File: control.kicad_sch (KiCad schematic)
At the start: 25 parts, among them U1 MX6UL-VM, Y1 24Mhz, Y2 32.768kHz

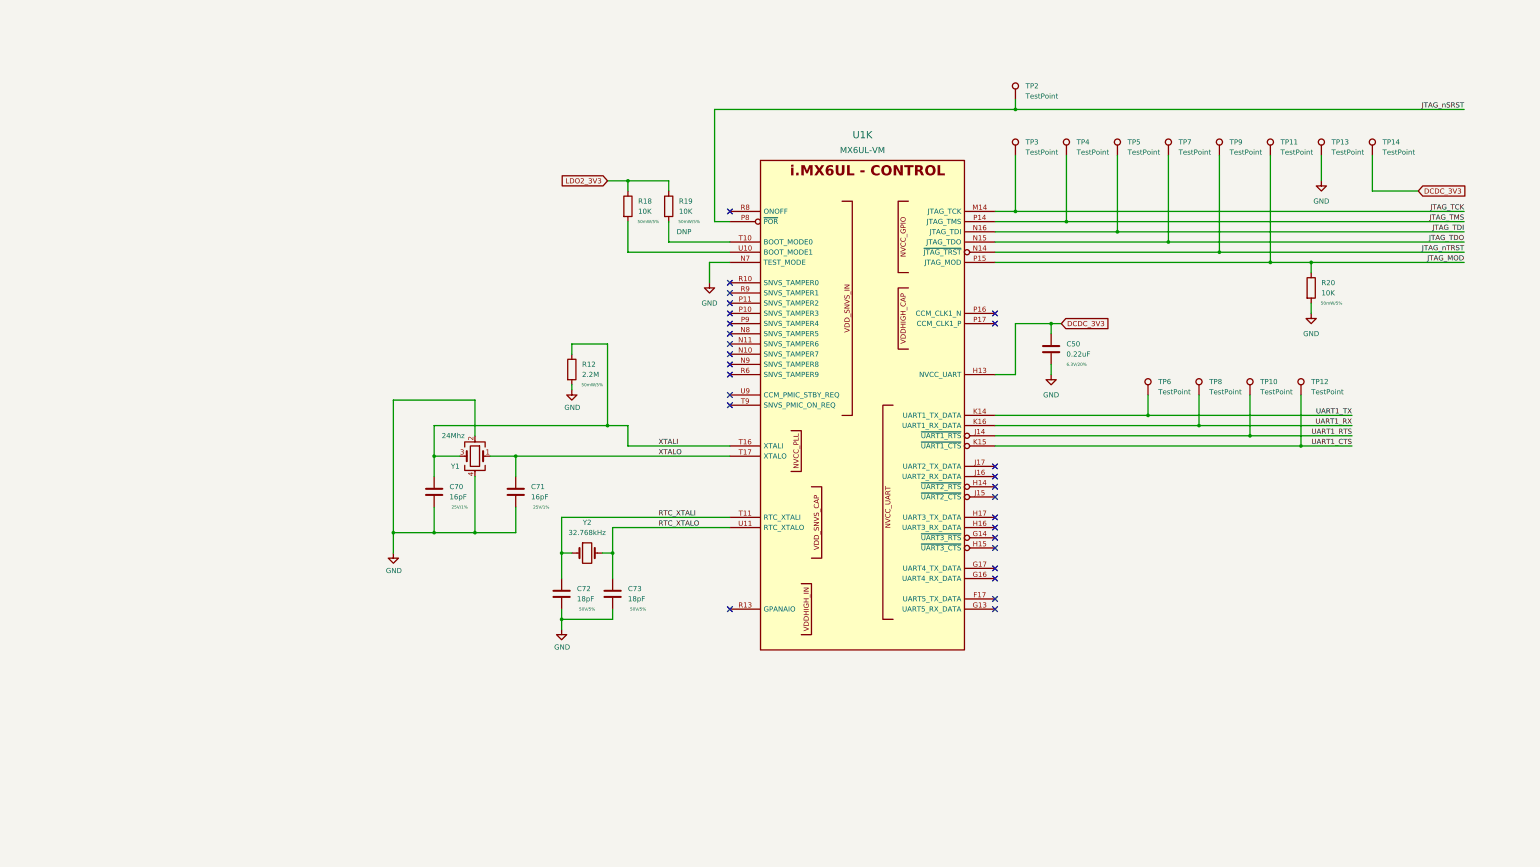
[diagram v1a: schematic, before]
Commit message: start moving to hierarchal labels, add emmc
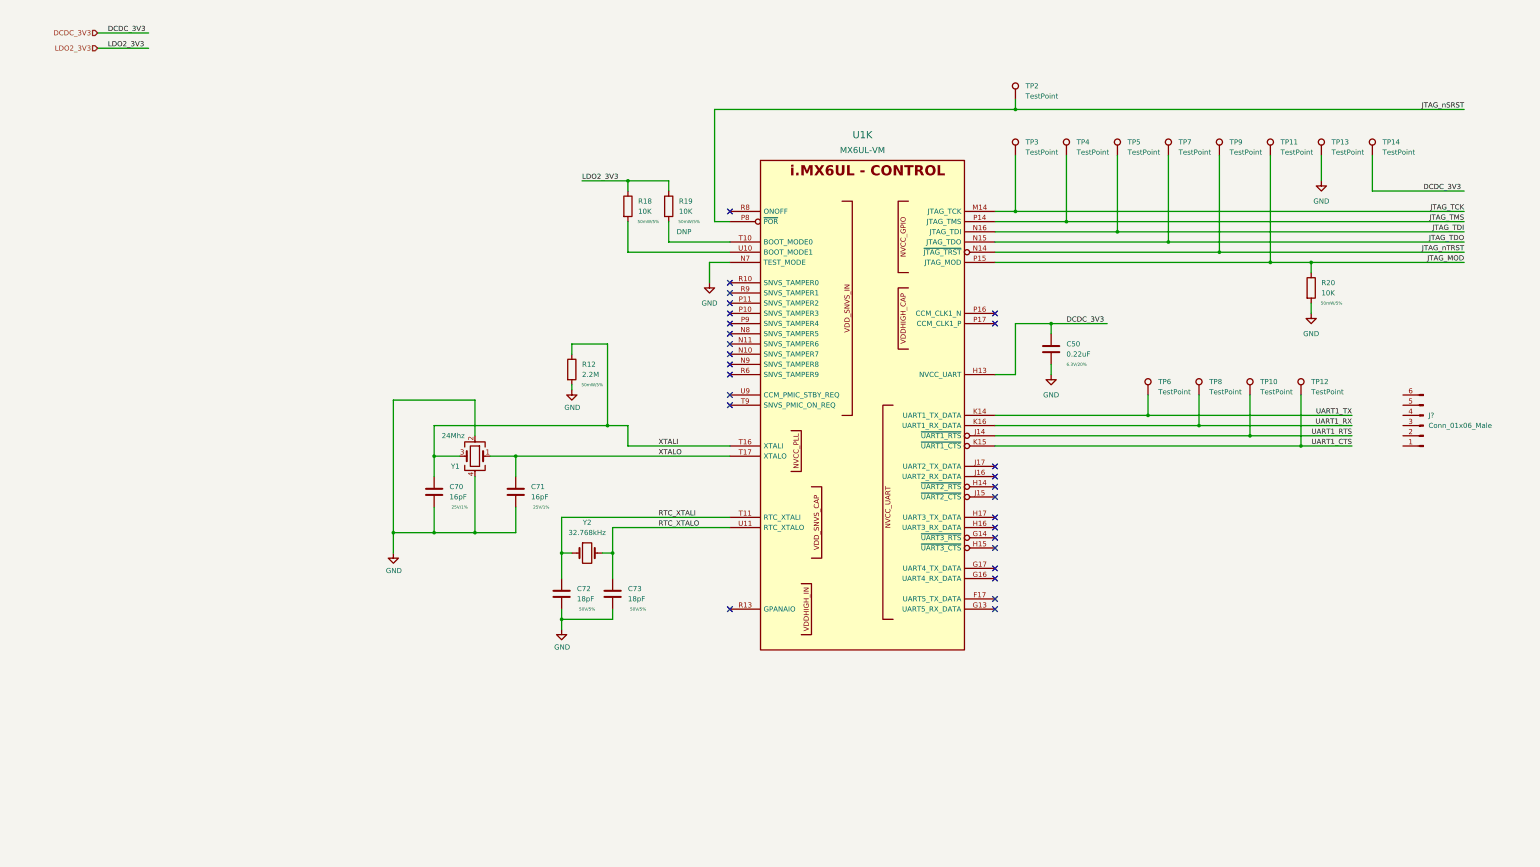
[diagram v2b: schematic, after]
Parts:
- added J?: Conn_01x06_Male, symbol Connector:Conn_01x06_Male
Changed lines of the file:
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@@
     (stroke (width 0) (type default) (color 0 0 0 0))
   )
-  (wire (pts (xy 361.95 60.96) (xy 350.52 60.96))
+  (wire (pts (xy 350.52 60.96) (xy 373.38 60.96))
     (stroke (width 0) (type default) (color 0 0 0 0))
   )
@@
     (stroke (width 0) (type default) (color 0 0 0 0))
   )
+  (wire (pts (xy 33.02 21.59) (xy 45.72 21.59))
+    (stroke (width 0) (type default) (color 0 0 0 0))
+  )
   (wire (pts (xy 294.64 111.76) (xy 294.64 116.84))
     (stroke (width 0) (type default) (color 0 0 0 0))
@@
     (stroke (width 0) (type default) (color 0 0 0 0))
   )
-  (wire (pts (xy 160.02 58.42) (xy 165.1 58.42))
+  (wire (pts (xy 153.67 58.42) (xy 165.1 58.42))
     (stroke (width 0) (type default) (color 0 0 0 0))
   )
@@
     (stroke (width 0) (type default) (color 0 0 0 0))
   )
-  (wire (pts (xy 273.05 93.98) (xy 270.51 93.98))
+  (wire (pts (xy 270.51 93.98) (xy 284.48 93.98))
     (stroke (width 0) (type default) (color 0 0 0 0))
   )
@@
   )
   (wire (pts (xy 270.51 93.98) (xy 261.62 93.98))
+    (stroke (width 0) (type default) (color 0 0 0 0))
+  )
+  (wire (pts (xy 33.02 25.4) (xy 45.72 25.4))
     (stroke (width 0) (type default) (color 0 0 0 0))
   )
@@
     (effects (font (size 1.27 1.27)) (justify right bottom))
   )
+  (label "DCDC_3V3" (at 363.22 60.96 0)
+    (effects (font (size 1.27 1.27)) (justify left bottom))
+  )
   (label "UART1_TX" (at 345.44 116.84 180)
     (effects (font (size 1.27 1.27)) (justify right bottom))
@@
     (effects (font (size 1.27 1.27)) (justify left bottom))
   )
+  (label "LDO2_3V3" (at 153.67 58.42 0)
+    (effects (font (size 1.27 1.27)) (justify left bottom))
+  )
   (label "UART1_RX" (at 345.44 119.38 180)
     (effects (font (size 1.27 1.27)) (justify right bottom))
@@
   (label "UART1_CTS" (at 345.44 124.46 180)
     (effects (font (size 1.27 1.27)) (justify right bottom))
+  )
+  (label "DCDC_3V3" (at 274.32 93.98 0)
+    (effects (font (size 1.27 1.27)) (justify left bottom))
   )
   (label "RTC_XTALO" (at 172.72 144.78 0)
@@
     (effects (font (size 1.27 1.27)) (justify right bottom))
   )
-  (global_label "DCDC_3V3" (shape input) (at 273.05 93.98 0) (fields_autoplaced)
-    (effects (font (size 1.27 1.27)) (justify left))
-    (property "Intersheet References" "${INTERSHEET_REFS}" (id 0) (at 285.0183 93.9006 0)
-      (effects (font (size 1.27 1.27)) (justify left) hide)
-    )
-  )
-  (global_label "LDO2_3V3" (shape input) (at 160.02 58.42 180) (fields_autoplaced)
+  (label "DCDC_3V3" (at 35.56 21.59 0)
+    (effects (font (size 1.27 1.27)) (justify left bottom))
+  )
+  (label "LDO2_3V3" (at 35.56 25.4 0)
+    (effects (font (size 1.27 1.27)) (justify left bottom))
+  )
+  (hierarchical_label "LDO2_3V3" (shape input) (at 33.02 25.4 180)
     (effects (font (size 1.27 1.27)) (justify right))
-    (property "Intersheet References" "${INTERSHEET_REFS}" (id 0) (at 148.2936 58.3406 0)
-      (effects (font (size 1.27 1.27)) (justify right) hide)
-    )
-  )
-  (global_label "DCDC_3V3" (shape input) (at 361.95 60.96 0) (fields_autoplaced)
-    (effects (font (size 1.27 1.27)) (justify left))
-    (property "Intersheet References" "${INTERSHEET_REFS}" (id 0) (at 373.9183 60.8806 0)
-      (effects (font (size 1.27 1.27)) (justify left) hide)
-    )
+  )
+  (hierarchical_label "DCDC_3V3" (shape input) (at 33.02 21.59 180)
+    (effects (font (size 1.27 1.27)) (justify right))
   )
   (symbol (lib_id "Device:R") (at 151.13 105.41 0) (unit 1)
@@
     (pin "1")
   )
+  (symbol (lib_id "Connector:Conn_01x06_Male") (at 363.22 119.38 180) (unit 1)
+    (in_bom yes) (on_board yes) (fields_autoplaced)
+    (property "Reference" "J?" (id 0) (at 364.49 116.8399 0)
+      (effects (font (size 1.27 1.27)) (justify right))
+    )
+    (property "Value" "Conn_01x06_Male" (id 1) (at 364.49 119.3799 0)
+      (effects (font (size 1.27 1.27)) (justify right))
+    )
+    (property "Footprint" "" (id 2) (at 363.22 119.38 0)
+      (effects (font (size 1.27 1.27)) hide)
+    )
+    (property "Datasheet" "~" (id 3) (at 363.22 119.38 0)
+      (effects (font (size 1.27 1.27)) hide)
+    )
+    (pin "1")
+    (pin "2")
+    (pin "3")
+    (pin "4")
+    (pin "5")
+    (pin "6")
+  )
   (symbol (lib_id "Device:R") (at 165.1 64.77 0) (unit 1)

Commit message: move to hierarchal labels, work on power tree, add basic pcb layout
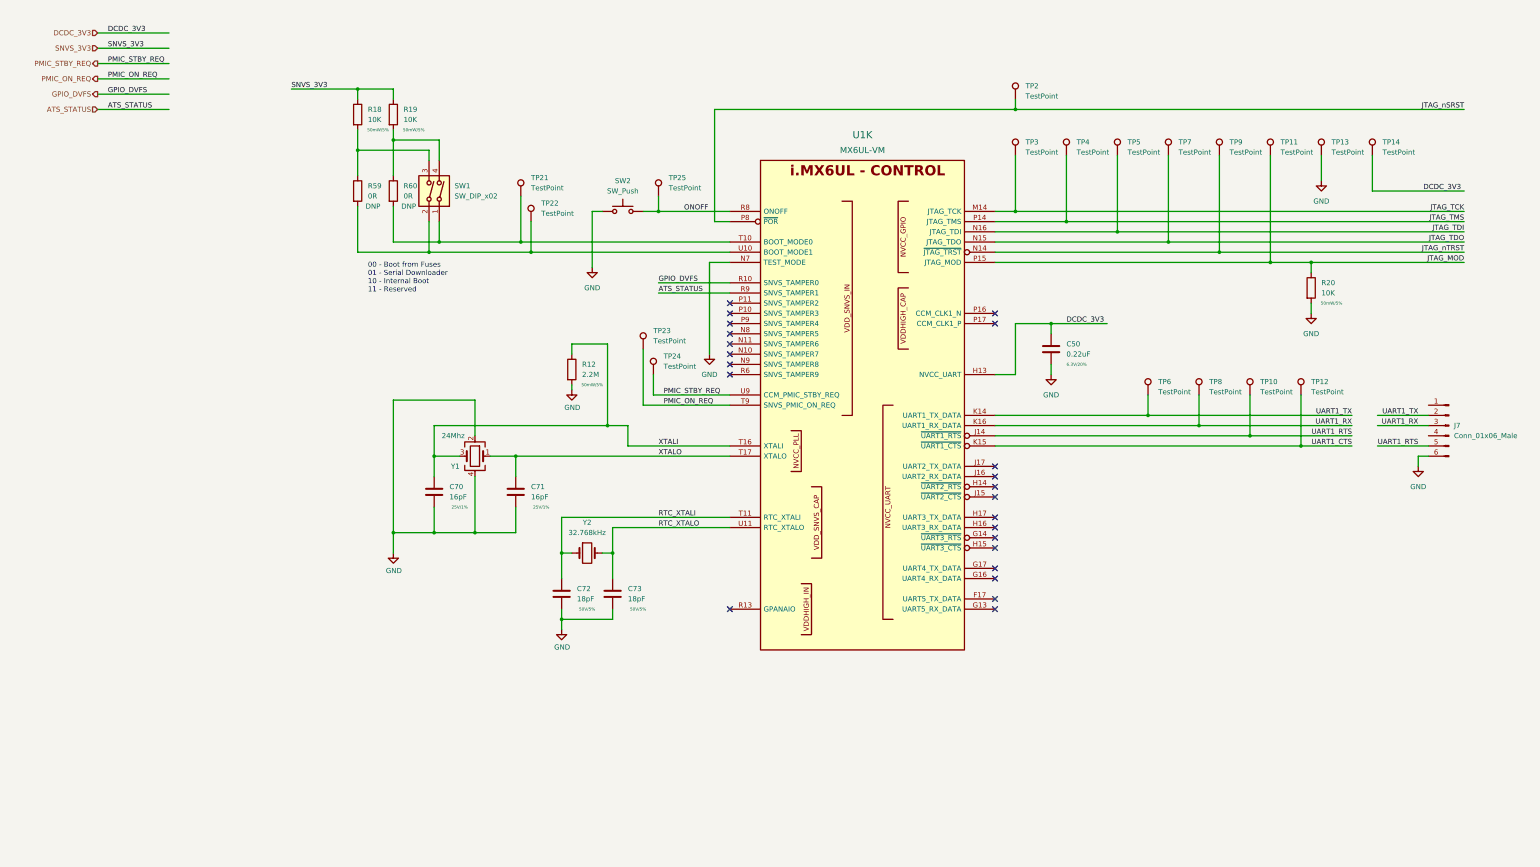
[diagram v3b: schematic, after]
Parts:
- added R59, R60: 0R, Resistor_SMD:R_0402_1005Metric, symbol Device:R
- added SW1: SW_DIP_x02, symbol Switch:SW_DIP_x02
- added SW2: SW_Push, symbol Switch:SW_Push
- added TP21, TP22, TP23, TP24, TP25: TestPoint, TestPoint:TestPoint_Pad_D1.0mm, symbol Connector:TestPoint
- C50: footprint Capacitor_SMD:C_0402_1005Metric -> Capacitor_SMD:C_0201_0603Metric
- J7: renamed from J?; footprint (none) -> Connector_PinHeader_2.54mm:PinHeader_1x06_P2.54mm_Vertical_SMD_Pin1Left
- R19: DNP DNP -> (none)
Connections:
- net GND: now also J7.6 (Pin_6), SW2.1
- net UART1_RTS: now also J7.5 (Pin_5)
- net UART1_RX: now also J7.3 (Pin_3)
- net UART1_TX: now also J7.2 (Pin_2)
- net at U1.T10 (BOOT_MODE0): now also R60.2, SW1.1, TP21.1; no longer R19.2
- net GPIO_DVFS: now reaches U1.R10 (SNVS_TAMPER0)
- net ONOFF: now reaches U1.R8 (ONOFF)
- net ONOFF: now also SW2.2, TP25.1
- net ATS_STATUS: now reaches U1.R9 (SNVS_TAMPER1)
- net PMIC_ON_REQ: now reaches U1.T9 (SNVS_PMIC_ON_REQ)
- net PMIC_ON_REQ: now also TP23.1
- net at U1.U10 (BOOT_MODE1): now also R59.2, SW1.2, TP22.1; no longer R18.2
- net PMIC_STBY_REQ: now reaches U1.U9 (CCM_PMIC_STBY_REQ)
- net PMIC_STBY_REQ: now also TP24.1
- net LDO2_3V3 renamed SNVS_3V3
- new net: R19.2, R60.1, SW1.4
- new net: R18.2, R59.1, SW1.3
- no-connect marks 28 -> 23
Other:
- note added: "00 - Boot from Fuses 01 - Serial Downloader 10 - Internal Boot 11 - Reserved"
- moved on the sheet: J7, R18, R19

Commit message: most of sch done, inital component pcb placement
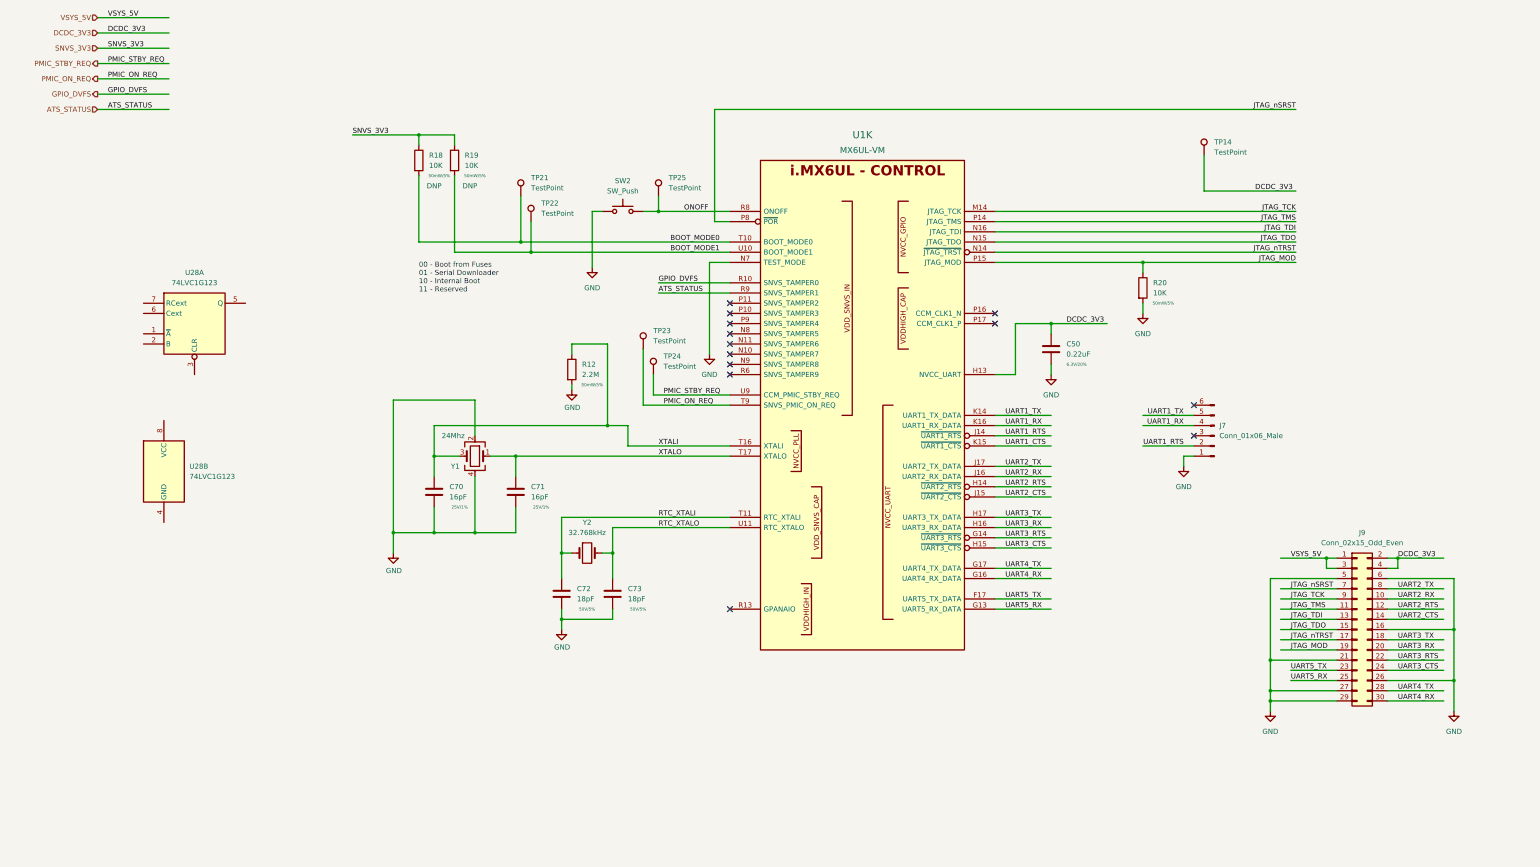
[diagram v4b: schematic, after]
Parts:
- removed R59, R60: 0R, Resistor_SMD:R_0402_1005Metric, symbol Device:R
- removed SW1: SW_DIP_x02, symbol Switch:SW_DIP_x02
- removed TP10, TP11, TP12, TP13, TP2, TP3, TP4, TP5, TP6, TP7, TP8, TP9: TestPoint, TestPoint:TestPoint_Pad_D1.0mm, symbol Connector:TestPoint
- added J9: Conn_02x15_Odd_Even, Connector_PinHeader_2.54mm:PinHeader_2x15_P2.54mm_Vertical_SMD, symbol Connector_Generic:Conn_02x15_Odd_Even
- added U28: 74LVC1G123, imx6ull-sbc:SOT1203, symbol 74xGxx:74LVC1G123
- J7: footprint Connector_PinHeader_2.54mm:PinHeader_1x06_P2.54mm_Vertical_SMD_Pin1Left -> Connector_Harwin:Harwin_M20-89006xx_1x06_P2.54mm_Horizontal
- R18, R19: DNP (none) -> DNP
- SW2: footprint (none) -> Button_Switch_THT:SW_Tactile_SPST_Angled_PTS645Vx58-2LFS
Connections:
- net DCDC_3V3: now also J9.2 (Pin_2), J9.4 (Pin_4)
- net GND: now also J7.1 (Pin_1), J9.16 (Pin_16), J9.21 (Pin_21), J9.26 (Pin_26), J9.27 (Pin_27), J9.29 (Pin_29), J9.5 (Pin_5), J9.6 (Pin_6); no longer J7.6 (Pin_6)
- net JTAG_MOD: now also J9.19 (Pin_19)
- net JTAG_TCK: now also J9.9 (Pin_9)
- net JTAG_TDI: now also J9.13 (Pin_13)
- net JTAG_TDO: now also J9.15 (Pin_15)
- net JTAG_TMS: now also J9.11 (Pin_11)
- net JTAG_nSRST: now also J9.7 (Pin_7)
- net JTAG_nTRST: now also J9.17 (Pin_17)
- net UART1_RTS: now also J7.2 (Pin_2); no longer J7.5 (Pin_5)
- net UART1_RX: now also J7.4 (Pin_4); no longer J7.3 (Pin_3)
- net UART1_TX: now also J7.5 (Pin_5); no longer J7.2 (Pin_2)
- net BOOT_MODE0: now reaches TP21.1, U1.T10 (BOOT_MODE0)
- net BOOT_MODE0: now also R18.2
- net BOOT_MODE1: now reaches TP22.1, U1.U10 (BOOT_MODE1)
- net BOOT_MODE1: now also R19.2
- net UART5_TX: now reaches U1.F17 (UART5_TX_DATA)
- net UART5_TX: now also J9.23 (Pin_23)
- net UART5_RX: now reaches U1.G13 (UART5_RX_DATA)
- net UART5_RX: now also J9.25 (Pin_25)
- net UART3_RTS: now reaches U1.G14 (~{UART3_RTS})
- net UART3_RTS: now also J9.22 (Pin_22)
- net UART4_RX: now reaches U1.G16 (UART4_RX_DATA)
- net UART4_RX: now also J9.30 (Pin_30)
- net UART4_TX: now reaches U1.G17 (UART4_TX_DATA)
- net UART4_TX: now also J9.28 (Pin_28)
- net UART2_RTS: now reaches U1.H14 (~{UART2_RTS})
- net UART2_RTS: now also J9.12 (Pin_12)
- net UART3_CTS: now reaches U1.H15 (~{UART3_CTS})
- net UART3_CTS: now also J9.24 (Pin_24)
- net UART3_RX: now reaches U1.H16 (UART3_RX_DATA)
- net UART3_RX: now also J9.20 (Pin_20)
- net UART3_TX: now reaches U1.H17 (UART3_TX_DATA)
- net UART3_TX: now also J9.18 (Pin_18)
- net UART2_CTS: now reaches U1.J15 (~{UART2_CTS})
- net UART2_CTS: now also J9.14 (Pin_14)
- net UART2_RX: now reaches U1.J16 (UART2_RX_DATA)
- net UART2_RX: now also J9.10 (Pin_10)
- net UART2_TX: now reaches U1.J17 (UART2_TX_DATA)
- net UART2_TX: now also J9.8 (Pin_8)
- new net VSYS_5V: J9.1 (Pin_1), J9.3 (Pin_3)
- no-connect marks 23 -> 13
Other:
- moved on the sheet: J7, R18, R19, R20, TP14
